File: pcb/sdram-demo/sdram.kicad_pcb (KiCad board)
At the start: 2 copper layers, 25 x 55 mm, 19 parts, among them U1 74HC595, U2 74HC595, U3 74HC595, U4 MT48LC16M16A2P, U5 Pico

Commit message: Update pcb
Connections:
- U5 pad 21: /SER1 -> unconnected-(U5-GPIO16-Pad21)
- U5 pad 26: unconnected-(U5-GPIO20-Pad26) -> /SER1
- U5 pad 27: /SRCLK -> /SER3
- U5 pad 30: unconnected-(U5-RUN-Pad30) -> /SRCLK
- U5 pad 31: /SER3 -> unconnected-(U5-GPIO26_ADC0-Pad31)
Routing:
- net /SER3: track 25.4 -> 41.1 mm
- net Net-(U3-QC): track 24.3 -> 28.2 mm
- net /RCLK: track 63.1 -> 66.1 mm
- net /SRCLK: track 68.0 -> 65.2 mm, vias 3 -> 4
- net GND: track 1.31 -> 3.96 mm, vias 7 -> 9
- net /SER1: track 21.5 -> 19.3 mm
- net +3V3: track 151.8 -> 152.9 mm
- net Net-(U1-QA): track 7.06 -> 8.09 mm
- net Net-(U1-QE): track 12.2 -> 13.1 mm
- net Net-(U1-QH): track 11.7 -> 12.7 mm
- net Net-(U1-QG): track 11.9 -> 12.8 mm
- net Net-(U1-QD): track 12.3 -> 13.3 mm
- net Net-(U1-QC): track 12.5 -> 13.4 mm
- net Net-(U1-QF): track 12.0 -> 13.0 mm

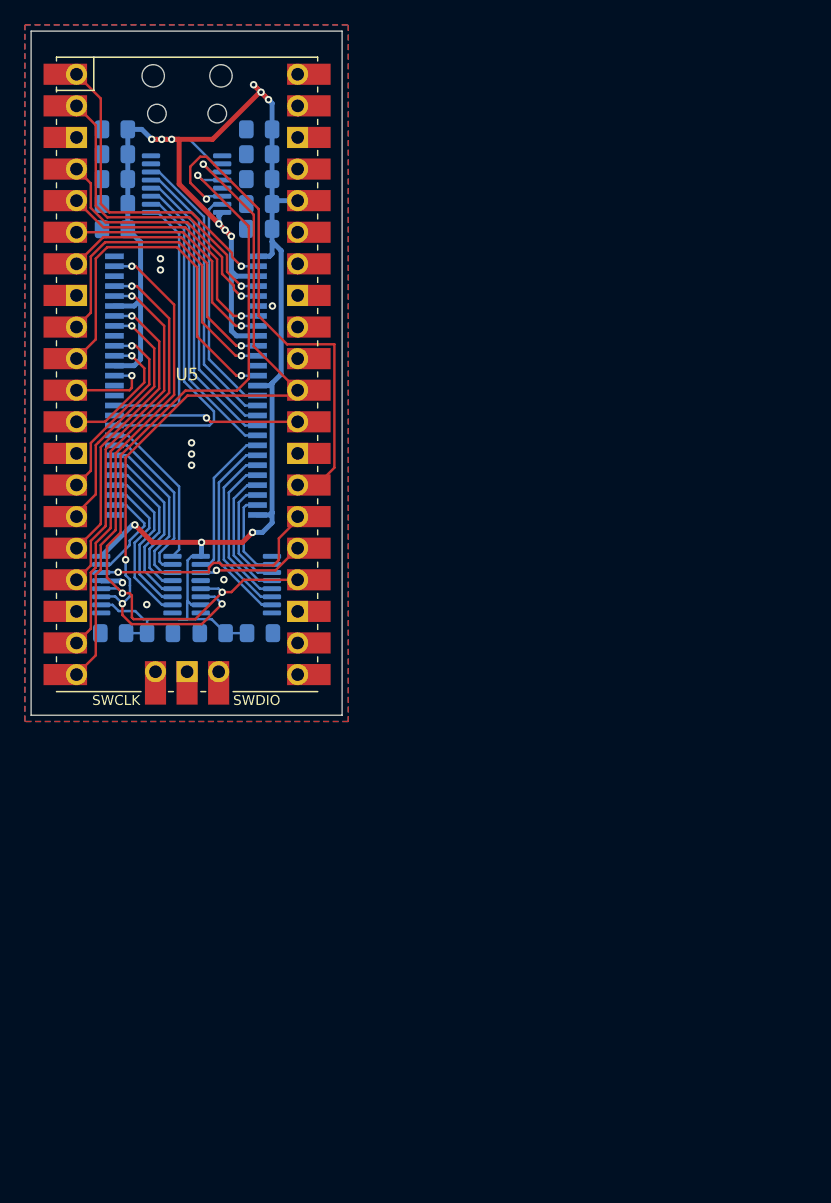
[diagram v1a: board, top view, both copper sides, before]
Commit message: Update pcb and add pio code
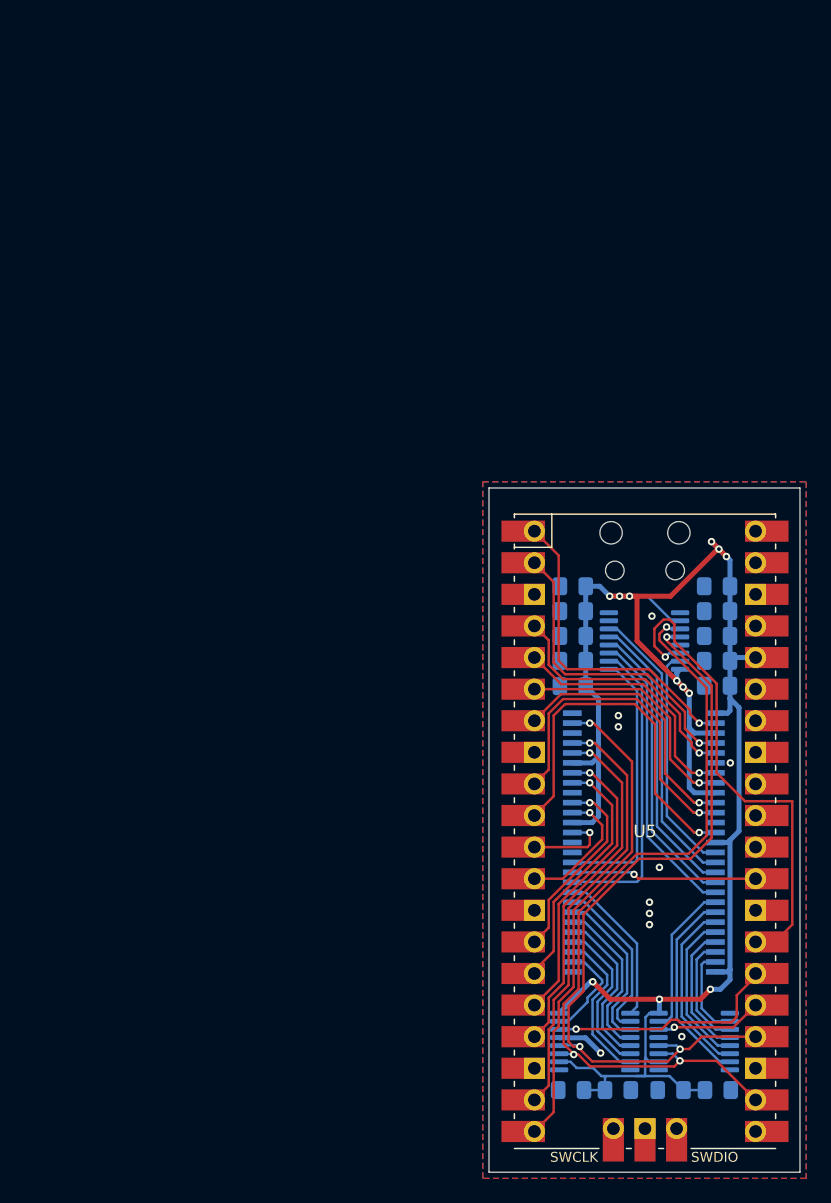
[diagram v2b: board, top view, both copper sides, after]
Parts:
- moved C1 52.0 mm to (26.9, 69.6)
- moved C10 52.0 mm to (27.0, 37.2)
- moved C11 52.0 mm to (27.0, 35.1)
- moved C12 52.0 mm to (27.0, 29.1)
- moved C13 52.0 mm to (27.0, 31.1)
- moved C14 52.0 mm to (27.0, 33.1)
- moved C2 52.0 mm to (30.7, 69.6)
- moved C4 52.0 mm to (38.7, 69.6)
- moved C5 52.0 mm to (38.6, 37.1)
- moved C6 52.0 mm to (38.6, 35.1)
- moved C7 52.0 mm to (38.6, 33.1)
- moved C8 52.0 mm to (38.6, 31.1)
- moved C9 52.0 mm to (38.6, 29.1)
- moved U1 52.0 mm to (28.8, 65.7)
- moved U2 52.0 mm to (36.8, 65.7)
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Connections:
- U5 pad 22: unconnected-(U5-GPIO17-Pad22) -> /SRCLK
- U5 pad 30: /SRCLK -> unconnected-(U5-RUN-Pad30)
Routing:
- net GND: track 3.96 -> 8.12 mm, vias 9 -> 10
- net Net-(U3-QC): track 28.2 -> 24.6 mm
- net /RCLK: track 66.1 -> 62.5 mm
- net /SER3: track 41.1 -> 39.8 mm
- net unconnected-(U5-RUN-Pad30): track 0.00 -> 0.61 mm
- net /SRCLK: track 65.2 -> 64.6 mm, vias 4 -> 3
